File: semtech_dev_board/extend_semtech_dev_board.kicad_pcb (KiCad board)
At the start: 2 copper layers, 27 parts, among them J1 Conn_02x10_Odd_Even, J2 Conn_02x10_Odd_Even, J3 Conn_02x10_Odd_Even, J4 Conn_02x02_Odd_Even, J5 Conn_02x02_Odd_Even, J6 Conn_02x02_Odd_Even, P0 Pin Hdr 2x10, P1 Pin Hdr 2x10, P2 Pin Hdr 2x10, P30 Pin Header 2x2 SMD, P31 Pin Header 2x2 SMD, P32 Pin Header 2x2 SMD

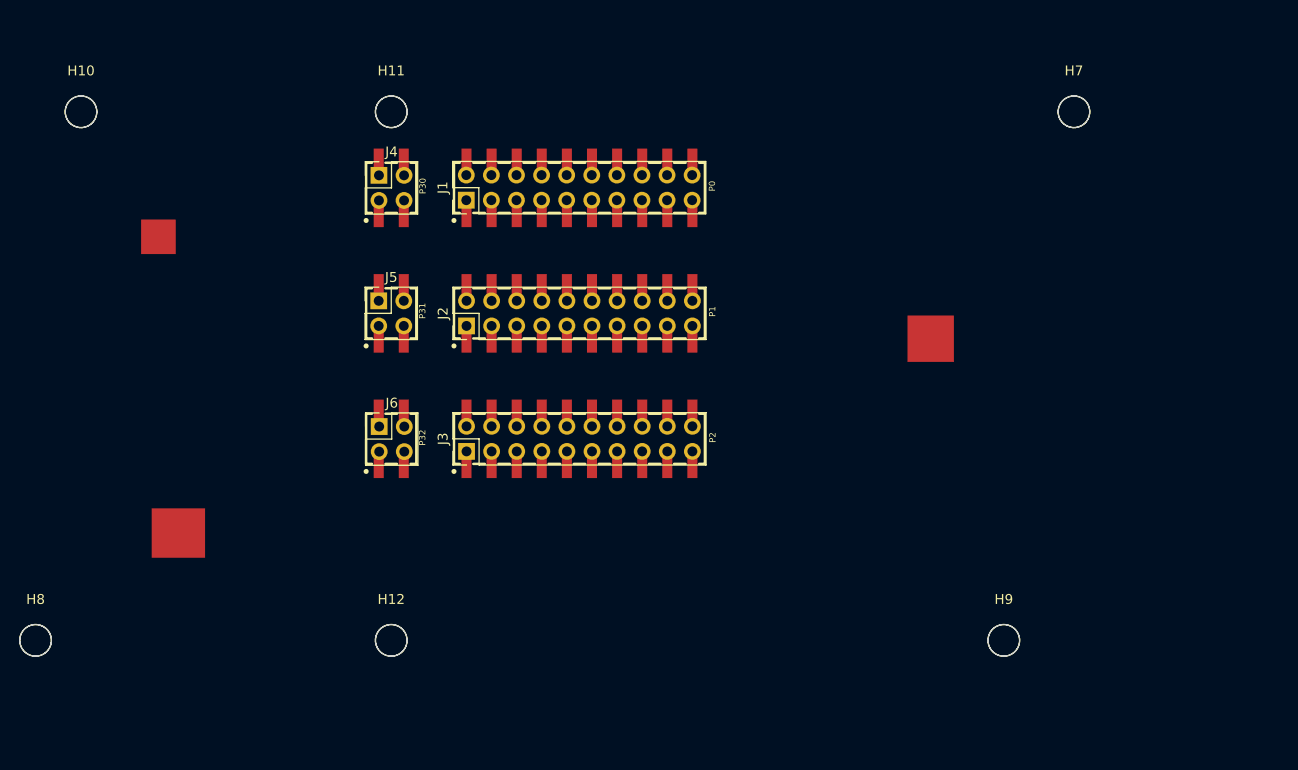
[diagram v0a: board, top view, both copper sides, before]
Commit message: starting point of design block
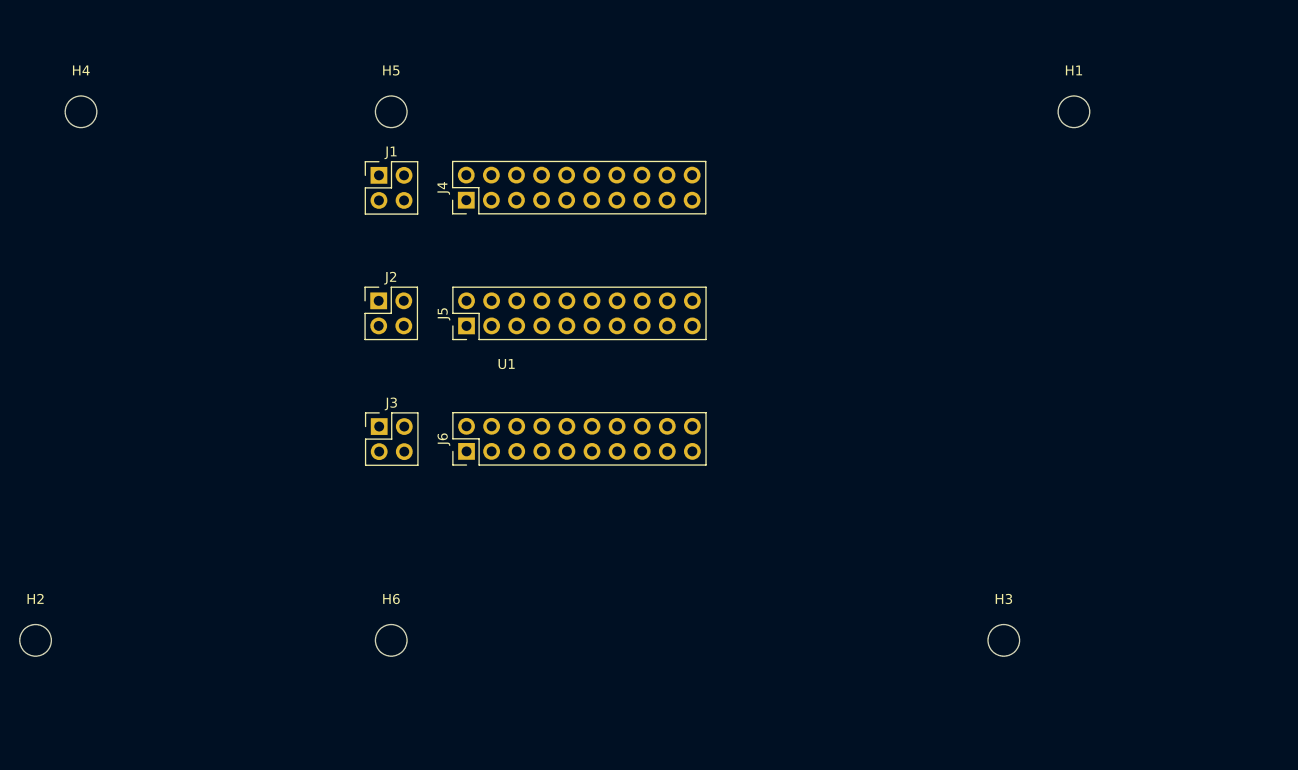
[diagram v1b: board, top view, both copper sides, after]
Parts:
- removed ? (x9): , 
- removed P0, P1, P2: Pin Hdr 2x10, Parts$:HDR_2x10-SMD
- removed P30, P31, P32: Pin Header 2x2 SMD, HDR_2x2-SMD:HDR_2x2-SMD
- added U1: ~, project_lib:drawing, F.Cu at (42.4, 46.9)
- renumbered H7 to H1, H8 to H2, H9 to H3, H10 to H4, H11 to H5, H12 to H6, J4 to J1, J5 to J2, J6 to J3, J1 to J4, J2 to J5, J3 to J6

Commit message: [fab] complete the design of semtech dev board
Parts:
- removed H2, H4: MountingHole, MountingHole:MountingHole_3.2mm_M3
- added C1: 10u, Capacitor_SMD:C_1206_3216Metric, F.Cu at (113.5, 56.2)
- added C2: 10u, Capacitor_SMD:C_1206_3216Metric, F.Cu at (116.1, 56.2)
- added C4: 1u, Capacitor_SMD:C_0603_1608Metric, F.Cu at (111.2, 60.7)
- added C5: 1u, Capacitor_SMD:C_0603_1608Metric, F.Cu at (118.2, 61.0)
- added C6: 100n, Capacitor_SMD:C_0603_1608Metric, F.Cu at (118.1, 62.6)
- added JP1: Jumper_2_Bridged, Connector_PinHeader_2.54mm:PinHeader_1x02_P2.54mm_Vertical, F.Cu at (107.2, 96.2)
- added JP2: Jumper_2_Bridged, Connector_PinHeader_2.54mm:PinHeader_1x02_P2.54mm_Vertical, F.Cu at (113.7, 96.2)
- added JP3: Jumper_2_Bridged, Connector_PinHeader_2.54mm:PinHeader_1x02_P2.54mm_Vertical, F.Cu at (100.5, 96.2)
- added JP4: Jumper_3_Bridged12, Connector_PinHeader_2.54mm:PinHeader_1x03_P2.54mm_Vertical, F.Cu at (112.1, 48.5)
- added RF1: BWSMA-KWE-Z001, lcsc_footprints:C496551_SMA-TH_BWSMA-KWE-Z001, F.Cu at (151.9, 62.0)
- added RF2: BWSMA-KWE-Z001, lcsc_footprints:C496551_SMA-TH_BWSMA-KWE-Z001, F.Cu at (151.9, 83.7)
- added U2: E80-900M2212S_C55338904, lcsc_footprints:C55338904_WIRELM-SMD_E80-900M2212S, F.Cu at (126.1, 76.5)
- added U3: E220-900M22S, lcsc_footprints:C2971736_WIRELM-SMD_22P-L20_0-W14_0-P1_27-BR, F.Cu at (123.3, 71.7)
- added U4: TLV75533PDBV, Package_TO_SOT_SMD:SOT-23-5, F.Cu at (114.2, 60.8)
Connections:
- net /nrf54l15-dk/P2.00 renamed /nrf54l15-dk/P2.00/QSPI_DIO3
- net /nrf54l15-dk/P2.01 renamed /nrf54l15-dk/P2.01/QSPI_CLK
- net /nrf54l15-dk/P2.02 renamed /nrf54l15-dk/P2.02/QSPI_DIO0
- net /nrf54l15-dk/P2.03 renamed /nrf54l15-dk/P2.03/QSPI_DIO2
- net /nrf54l15-dk/P2.04 renamed /nrf54l15-dk/P2.04/QSPI_DIO1
- net /nrf54l15-dk/P2.05 renamed /nrf54l15-dk/P2.05/QSPI_CS
- J1 pad 1: +5V -> GND
- J1 pad 3: unconnected-(J1-Pin_3-Pad3) -> +5V
- J1 pad 4: GND -> unconnected-(J1-Pin_4-Pad4)
- J2 pad 1: +5V -> GND
- J2 pad 3: unconnected-(J2-Pin_3-Pad3) -> +5V
- J2 pad 4: GND -> unconnected-(J2-Pin_4-Pad4)
- J3 pad 1: +5V -> GND
- J3 pad 3: unconnected-(J3-Pin_3-Pad3) -> +5V
- J3 pad 4: GND -> unconnected-(J3-Pin_4-Pad4)
- J6 pad 10: /nrf54l15-dk/P2.07 -> /NRST
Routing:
- net +5V: track 0.00 -> 96.3 mm, vias 0 -> 8
- net /nrf54l15-dk/P0.00: track 0.00 -> 58.2 mm, vias 0 -> 2
- net /nrf54l15-dk/P1.09: track 0.00 -> 56.5 mm
- net /NRST: track 0.00 -> 42.8 mm
- net /nrf54l15-dk/P1.08: track 0.00 -> 42.4 mm
- net /nrf54l15-dk/P2.06: track 0.00 -> 40.3 mm
- net /nrf54l15-dk/P2.10: track 0.00 -> 39.3 mm, vias 0 -> 1
- net /P1.10/DIO/RXEN: track 0.00 -> 38.8 mm, vias 0 -> 1
- net /nrf54l15-dk/P2.08: track 0.00 -> 36.4 mm
- net /P1.09/DIO: track 0.00 -> 36.4 mm, vias 0 -> 1
- net /nrf54l15-dk/P2.09: track 0.00 -> 36.1 mm
- net /P1.08/DIO: track 0.00 -> 35.5 mm, vias 0 -> 1
- net /nrf54l15-dk/P1.10: track 0.00 -> 31.5 mm
- net /EN: track 0.00 -> 15.6 mm, vias 0 -> 2
- net +3V3: track 0.00 -> 13.0 mm
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- added copper zone on B.Cu, net GND
- added copper zone on F.Cu, net GND
- added copper zone on In1.Cu, net GND
- added copper zone on In2.Cu, net GND
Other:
- board outline added: 90 x 63.4 mm
- copper layers 2 -> 4
- board text added: "2.4GHz Port"
- board text added: "Compatible with NRF54L15 DK"
- board text added: "E220/E22"
- board text added: "E80"
- board text added: "LDO ENABLE"
- board text added: "P1.08"
- board text added: "P1.09"
- board text added: "P1.10"
- board text added: "Semtech/EBYTE evaluation board Designer: Kelvin Zhao Date: 2026.08 Version: v0.0.1"
- board text added: "Sub-GHz Port"
